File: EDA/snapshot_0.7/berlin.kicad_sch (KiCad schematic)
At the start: 441 parts, among them J201 TYPE-C-31-M12_13, J202 Conn_ARM_JTAG_SWD_10, J203 LCDCON, Q701 DTC123J, SW1,1 Rotary_Encoder_Switch_Chassis, SW1,10 MXSwitch, SW1,11 MXSwitch, SW1,12 MXSwitch, SW1,13 MXSwitch, SW1,14 MXSwitch, SW1,15 MXSwitch, SW1,16 Rotary_Encoder_Switch_Chassis, SW1,2 MXSwitch, SW1,3 MXSwitch, SW1,4 MXSwitch, SW1,5 MXSwitch, SW1,6 MXSwitch, SW1,7 MXSwitch, SW1,8 MXSwitch, SW1,9 MXSwitch, SW2,1 MXSwitch, SW2,10 MXSwitch, SW2,11 MXSwitch, SW2,12 MXSwitch, SW2,13 MXSwitch, SW2,14 MXSwitch, SW2,15 MXSwitch, SW2,16 MXSwitch, SW2,17 MXSwitch, SW2,18 MXSwitch, SW2,19 MXSwitch, SW2,2 MXSwitch, SW2,3 MXSwitch, SW2,4 MXSwitch, SW2,5 MXSwitch, SW2,6 MXSwitch, SW2,7 MXSwitch, SW2,8 MXSwitch, SW2,9 MXSwitch, SW201 SW_Push, SW3,1 MXSwitch, SW3,10 MXSwitch, SW3,11 MXSwitch, SW3,12 MXSwitch, SW3,13 MXSwitch, SW3,14 MXSwitch, SW3,15 MXSwitch, SW3,16 MXSwitch, SW3,17 MXSwitch, SW3,18 MXSwitch, SW3,19 MXSwitch, SW3,2 MXSwitch, SW3,3 MXSwitch, SW3,4 MXSwitch, SW3,5 MXSwitch, SW3,6 MXSwitch, SW3,7 MXSwitch, SW3,8 MXSwitch, SW3,9 MXSwitch, SW4,1 MXSwitch, SW4,10 MXSwitch, SW4,11 MXSwitch, SW4,12 MXSwitch, SW4,13 MXSwitch, SW4,14 MXSwitch, SW4,15 MXSwitch, SW4,16 MXSwitch, SW4,17 MXSwitch, SW4,18 MXSwitch, SW4,19 MXSwitch, SW4,2 MXSwitch, SW4,3 MXSwitch, SW4,4 MXSwitch, SW4,5 MXSwitch, SW4,6 MXSwitch, SW4,7 MXSwitch, SW4,8 MXSwitch, SW4,9 MXSwitch, SW5,1 MXSwitch, SW5,10 MXSwitch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

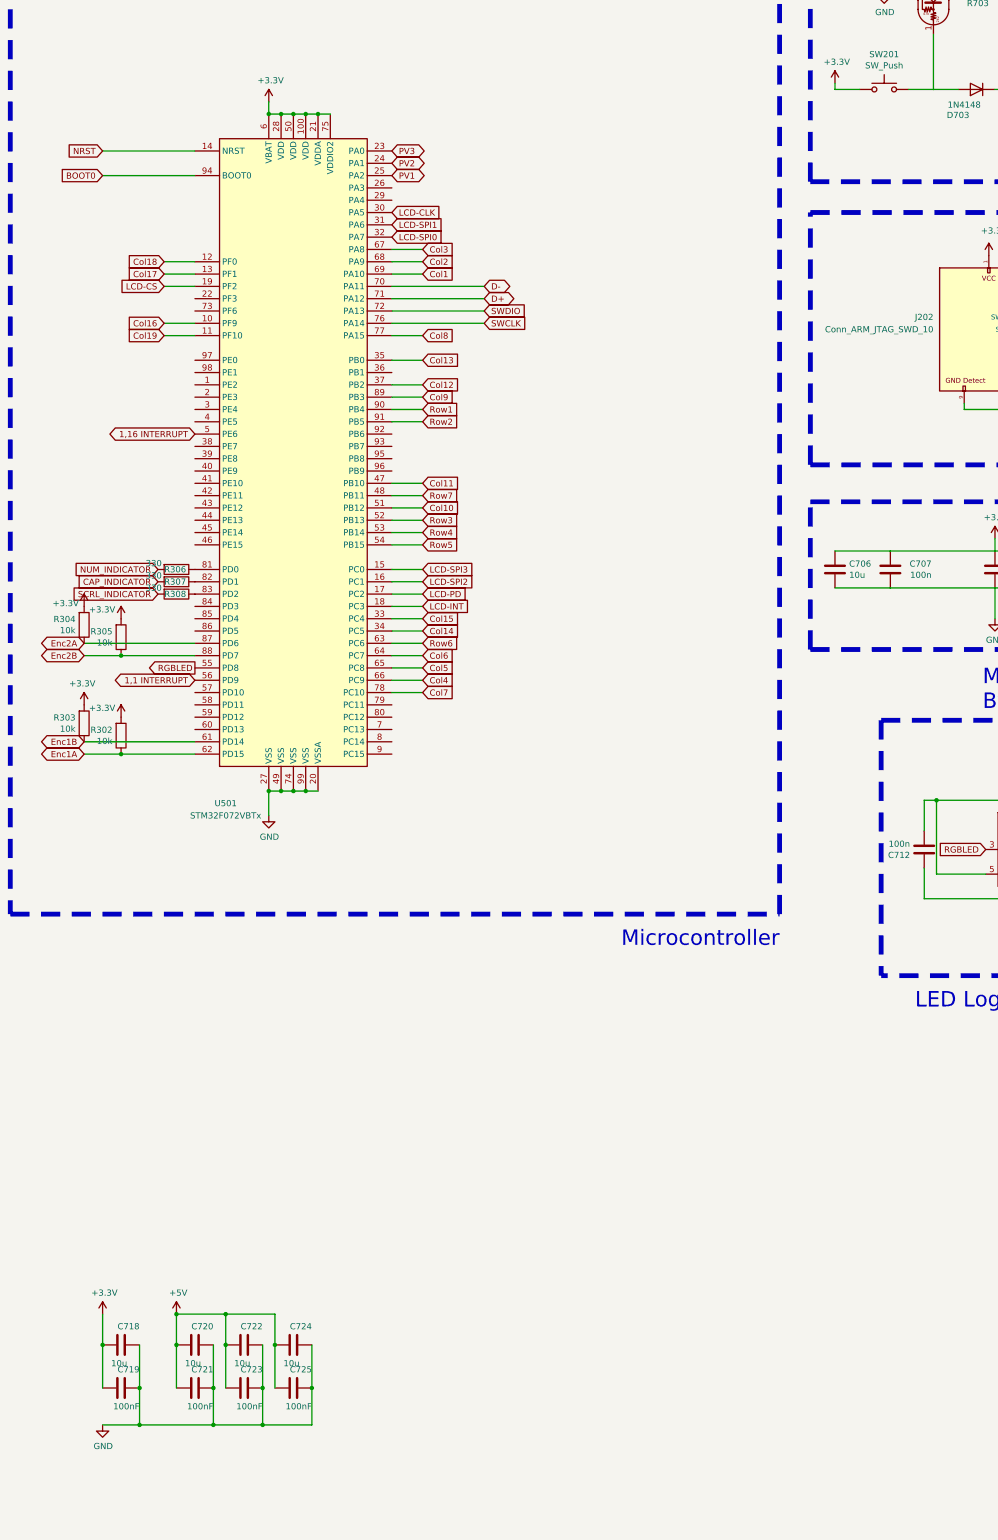
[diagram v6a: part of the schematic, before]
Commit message: 0.7: add second res button; bugfixes
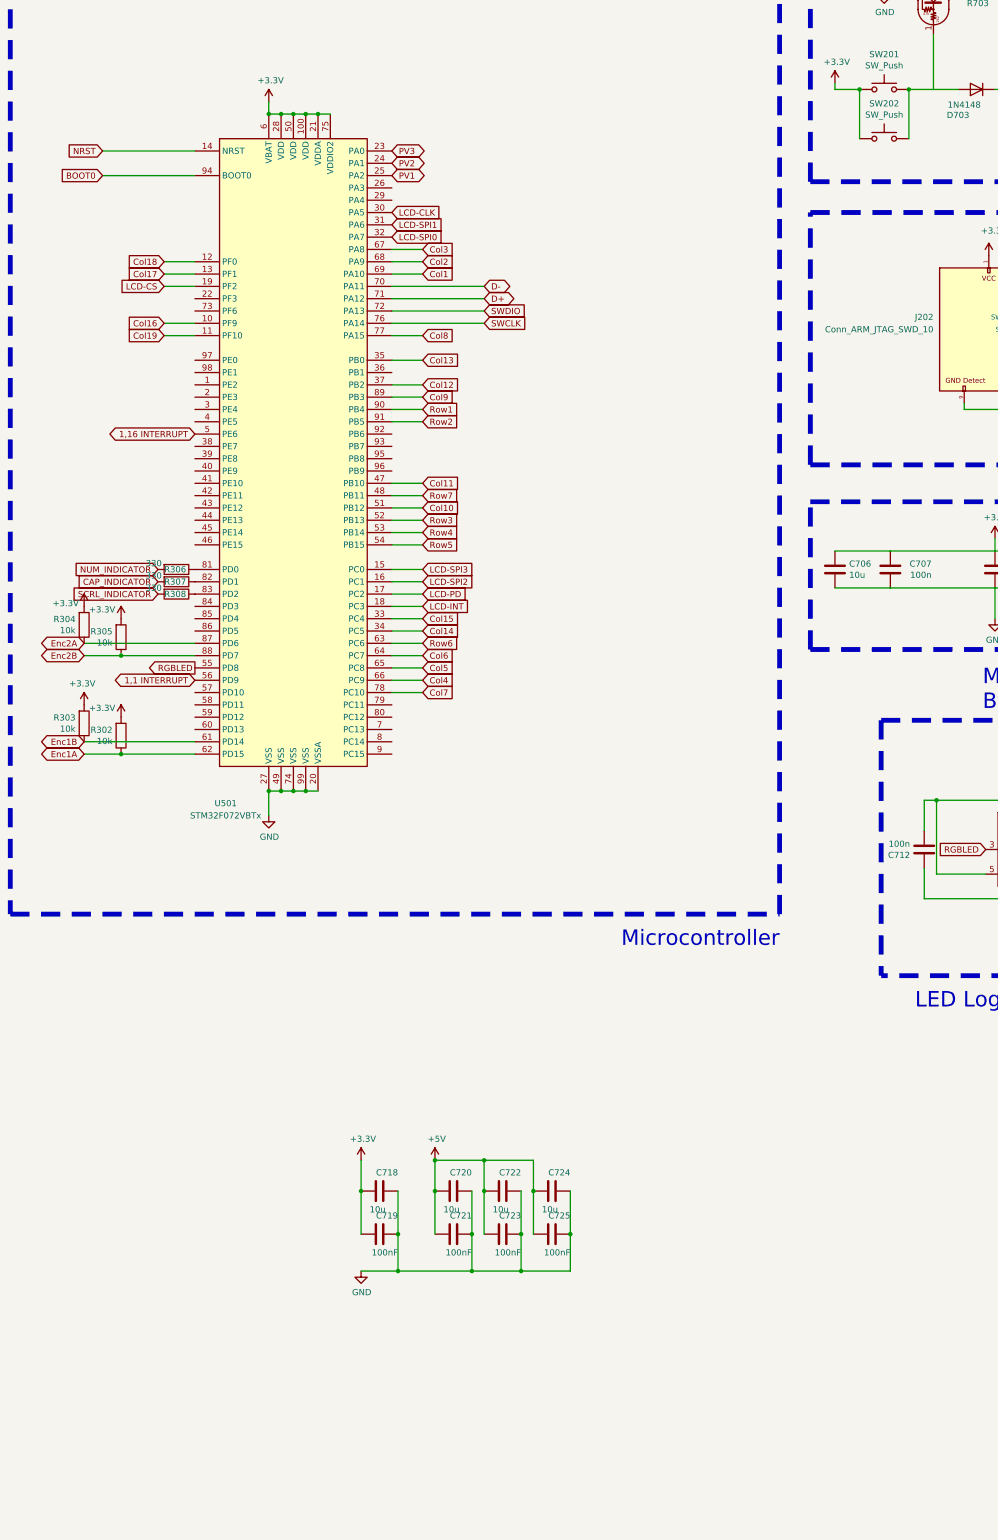
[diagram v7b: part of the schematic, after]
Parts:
- added SW202: SW_Push, Button_Switch_THT:SW_PUSH_6mm_H5mm, symbol Switch:SW_Push
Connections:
- net +3V3: now also SW202.1
- net at D703.2 (A), Q701.1 (B), SW201.2: now also SW202.2
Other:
- moved on the sheet: C718, C719, C720, C721, C722, C723, C724, C725

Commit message: fix 0.7 DRC issues, DRC rules
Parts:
- added C726: 10u, Capacitor_SMD:C_1206_3216Metric_Pad1.42x1.75mm_HandSolder, symbol Device:C
- added C727: 100nF, Capacitor_SMD:C_0805_2012Metric_Pad1.15x1.40mm_HandSolder, symbol Device:C
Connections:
- net +5V: now also C726.1, C727.1
- net GND: now also C726.2, C727.2
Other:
- note added: "LED Smoothing/ Bypass caps"
- moved on the sheet: C718, C719, C720, C721, C722, C723, C724, C725
